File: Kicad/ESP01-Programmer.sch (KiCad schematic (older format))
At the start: 6 parts, among them J1 Power Connector, J2 FTDI, U1 ESP-01v090

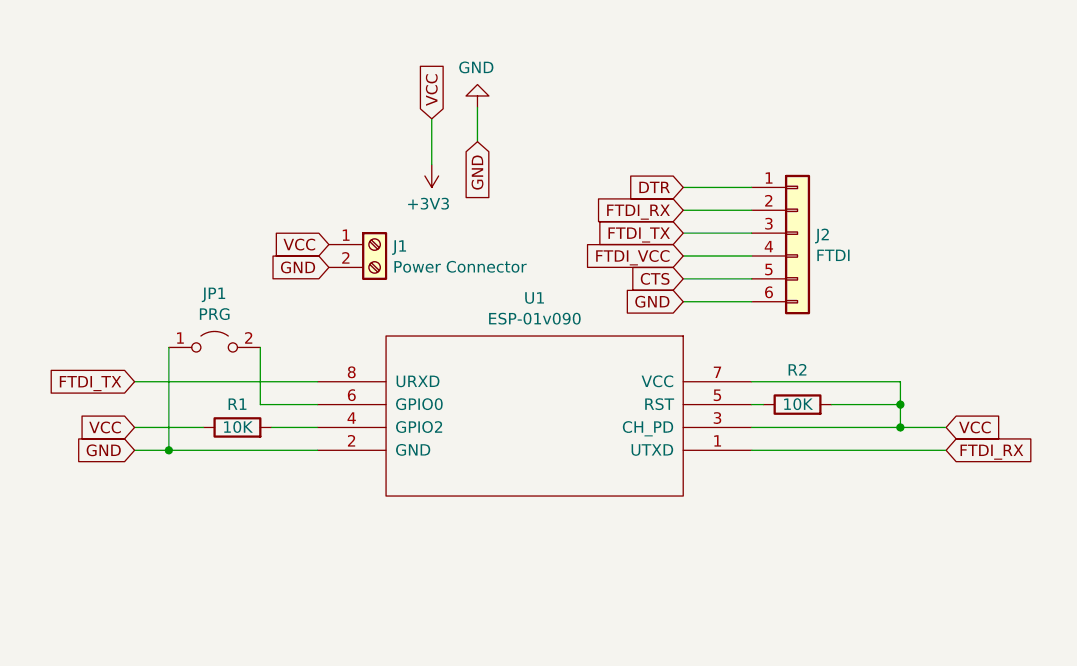
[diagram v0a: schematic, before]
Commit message: V1.1: Adding I2C bus headers.
More information and resources are also added.
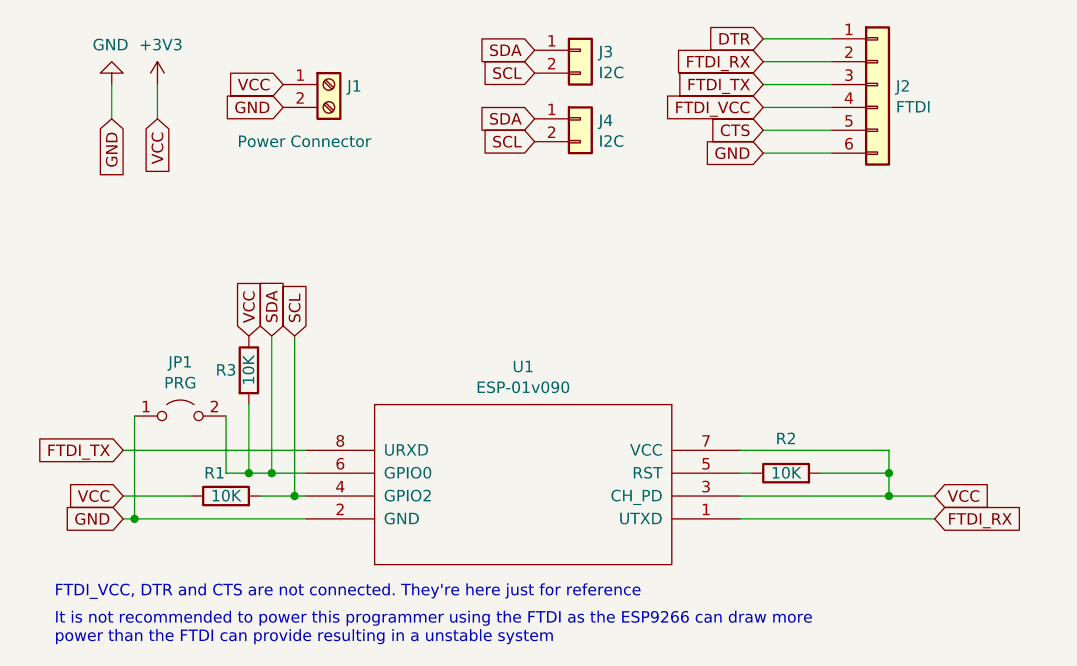
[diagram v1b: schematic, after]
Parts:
- added J3, J4: I2C, Connector_PinHeader_2.54mm:PinHeader_1x02_P2.54mm_Vertical, symbol Connector_Generic:Conn_01x02
- added R3: 10K, Resistor_THT:R_Axial_DIN0207_L6.3mm_D2.5mm_P10.16mm_Horizontal, symbol Device:R
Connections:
- net +3V3: now also R3.1
- net SCL: now reaches R1.2, U1.4 (GPIO2)
- net SCL: now also J3.2 (Pin_2), J4.2 (Pin_2)
- net SDA: now reaches JP1.2 (B), U1.6 (GPIO0)
- net SDA: now also J3.1 (Pin_1), J4.1 (Pin_1), R3.2
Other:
- note added: "FTDI_VCC, DTR and CTS are not connected. They're here just for reference"
- note added: "It is not recommended to power this programmer using the FTDI as the ESP9266 can draw more\npower than the FTDI can provide resulting in a unstable system"
- moved on the sheet: J1, J2, JP1, R1, R2, U1
